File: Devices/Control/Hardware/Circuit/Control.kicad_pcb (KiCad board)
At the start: 2 copper layers, 53 parts, among them J1 Screw_Terminal_01x03, J2 Screw_Terminal_01x03, J3 Conn_01x04, J4 Conn_01x04, J5 Conn_01x04, J6 AVR-ISP-6, J7 TYPE-C-31-M-12, J8 TYPE-C-31-M-12, Q1 Q_NPN_BCE, SW1 SW_Push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

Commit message: First control PCB
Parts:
- removed the D2 at (31.2, 132.4)
- added C9: 100n, Capacitor_SMD:C_0805_2012Metric_Pad1.18x1.45mm_HandSolder, B.Cu at (176.0, 7.54)
- added R11: 10k, Resistor_SMD:R_0805_2012Metric_Pad1.20x1.40mm_HandSolder, B.Cu at (144.0, -5.66)
- added R12: 10k, Resistor_SMD:R_0805_2012Metric_Pad1.20x1.40mm_HandSolder, B.Cu at (176.0, -5.66)
- added R13: 10k, Resistor_SMD:R_0805_2012Metric_Pad1.20x1.40mm_HandSolder, B.Cu at (176.0, 0.94)
- C2, C4, JP1, JP10, JP11, JP12, JP13, JP14, JP15, JP16, JP2, JP3, JP4, JP5, JP6, JP7, JP8, JP9, R2, R7, U2, U3: moved to B.Cu
- moved R6 247.0 mm to (199.6, -25.8), turned to 270 degrees
- moved D2 245.8 mm to (194.5, -25.8), turned to 90 degrees
- moved JP15 224.2 mm to (177.3, -21.0)
- moved JP16 223.0 mm to (177.3, -15.8), turned to 180 degrees
- moved SW2 222.7 mm to (197.1, -30.4)
- moved JP13 221.9 mm to (169.7, -21.0)
- moved JP14 220.8 mm to (169.7, -15.8), turned to 180 degrees
- moved J7 213.5 mm to (160.3, -35.0), turned to 180 degrees
- moved JP11 212.2 mm to (150.6, -21.0), turned to 180 degrees
- moved JP12 211.0 mm to (150.6, -15.8)
- moved J6 208.6 mm to (182.2, 15.2)
- moved C3 206.2 mm to (144.0, -5.66)
- moved U4 202.7 mm to (160.3, -16.3)
- moved R2 200.3 mm to (144.0, 0.94), turned to 180 degrees
- moved C1 198.1 mm to (144.0, 10.1)
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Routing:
- net GND: track 0.00 -> 483.2 mm, vias 0 -> 14
- net VCC: track 0.00 -> 312.8 mm, vias 0 -> 7
- net RST: track 0.00 -> 163.7 mm, vias 0 -> 1
- net EXTRX: track 0.00 -> 147.7 mm, vias 0 -> 1
- net EXTTX: track 0.00 -> 120.5 mm, vias 0 -> 2
- net SCL: track 0.00 -> 100.3 mm, vias 0 -> 2
- net EXTRST: track 0.00 -> 97.9 mm
- net RX: track 0.00 -> 89.0 mm, vias 0 -> 1
- net SDA: track 0.00 -> 87.1 mm, vias 0 -> 1
- net XTAL1: track 0.00 -> 86.2 mm
- net TX: track 0.00 -> 65.6 mm, vias 0 -> 1
- net SIG1A: track 0.00 -> 48.9 mm
- net SIG1B: track 0.00 -> 48.4 mm
- net SIG2A: track 0.00 -> 43.9 mm, vias 0 -> 2
- net SIG2B: track 0.00 -> 43.5 mm, vias 0 -> 2
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- added copper zone on B.Cu, net GND
- added copper zone on F.Cu, net GND
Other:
- board outline added: 82.5 x 73 mm

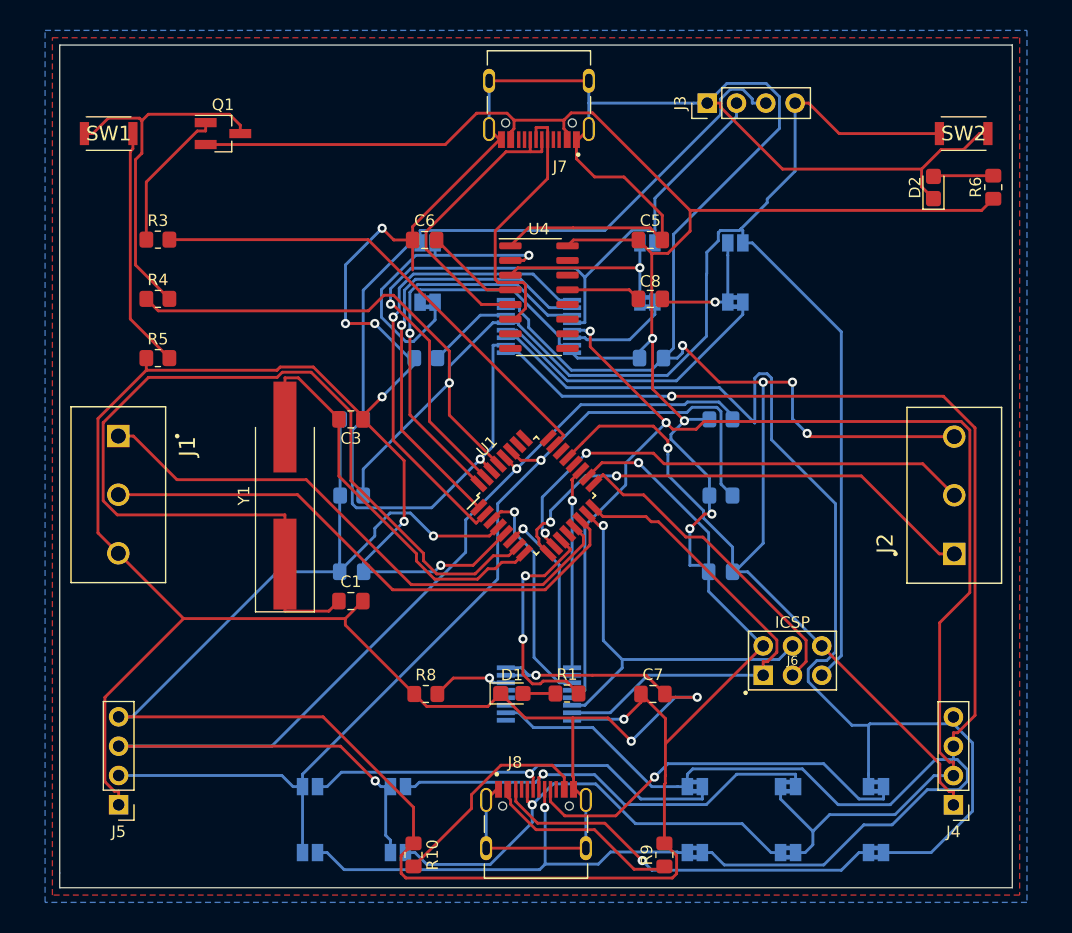
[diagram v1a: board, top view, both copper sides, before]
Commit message: Add mounting holes & component description
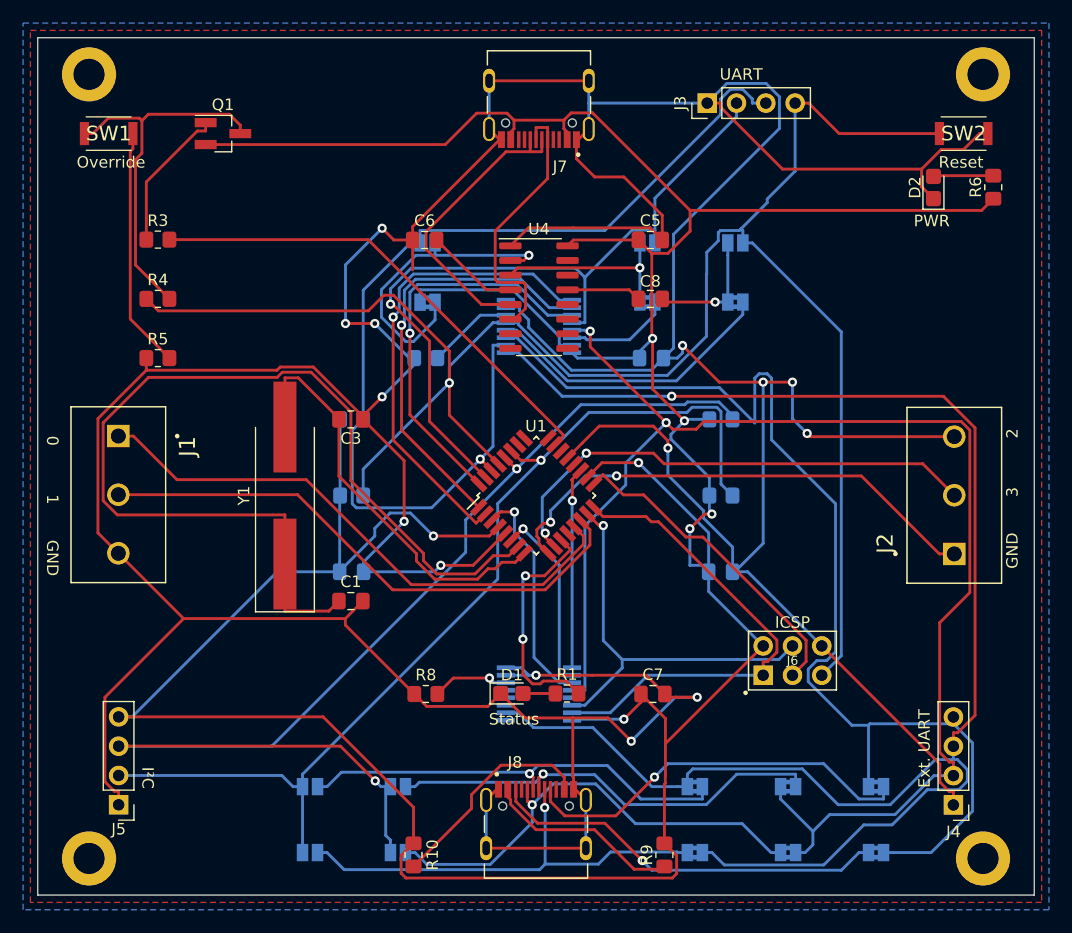
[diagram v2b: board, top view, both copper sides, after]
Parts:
- added MNT1: MountingHole_2.7mm_M2.5_DIN965_Pad, MountingHole:MountingHole_2.7mm_M2.5_DIN965_Pad, F.Cu at (198.8, 32.4)
- added MNT2: MountingHole_2.7mm_M2.5_DIN965_Pad, MountingHole:MountingHole_2.7mm_M2.5_DIN965_Pad, F.Cu at (121.3, 32.4)
- added MNT3: MountingHole_2.7mm_M2.5_DIN965_Pad, MountingHole:MountingHole_2.7mm_M2.5_DIN965_Pad, F.Cu at (121.3, -35.6)
- added MNT4: MountingHole_2.7mm_M2.5_DIN965_Pad, MountingHole:MountingHole_2.7mm_M2.5_DIN965_Pad, F.Cu at (198.8, -35.6)
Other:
- board size 82.5 x 73 mm -> 86.4 x 74.3 mm
- board text added: "0"
- board text added: "1"
- board text added: "2"
- board text added: "3"
- board text added: "Ext. UART"
- board text added: "GND"
- board text added: "I²C"
- board text added: "Override"
- board text added: "PWR"
- board text added: "Reset"
- board text added: "Status"
- board text added: "UART"
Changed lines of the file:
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@@
   (general
     (thickness 1.6)
-    (drawings 5)
+    (drawings 17)
     (tracks 858)
     (zones 0)
-    (modules 56)
+    (modules 60)
     (nets 78)
   )
@@
     (47 F.CrtYd user)
     (48 B.Fab user)
-    (49 F.Fab user)
+    (49 F.Fab user hide)
   )
   (setup
@@
     (add_net XTAL2)
   )
+  (module MountingHole:MountingHole_2.7mm_M2.5_DIN965_Pad (layer F.Cu)
+    (at 198.755 -35.56)
+    (descr "Mounting Hole 2.7mm, M2.5, DIN965")
+    (tags "mounting hole 2.7mm m2.5 din965")
+    (attr virtual)
+    (fp_text reference MNT4 (at 0 -3.35) (layer F.SilkS) hide
+      (effects (font (size 1 1) (thickness 0.15)))
+    )
+    (fp_text value MountingHole_2.7mm_M2.5_DIN965_Pad (at 0 3.35) (layer F.Fab)
+      (effects (font (size 1 1) (thickness 0.15)))
+    )
+    (fp_circle (center 0 0) (end 2.35 0) (layer Cmts.User) (width 0.15))
+    (fp_circle (center 0 0) (end 2.6 0) (layer F.CrtYd) (width 0.05))
+    (fp_text user %R (at 0.3 0) (layer F.Fab)
+      (effects (font (size 1 1) (thickness 0.15)))
+    )
+    (pad 1 thru_hole circle (at 0 0) (size 4.7 4.7) (drill 2.7) (layers *.Cu *.Mask))
+  )
+  (module MountingHole:MountingHole_2.7mm_M2.5_DIN965_Pad (layer F.Cu)
+    (at 121.285 -35.56)
+    (descr "Mounting Hole 2.7mm, M2.5, DIN965")
+    (tags "mounting hole 2.7mm m2.5 din965")
+    (attr virtual)
+    (fp_text reference MNT3 (at 0 -3.35) (layer F.SilkS) hide
+      (effects (font (size 1 1) (thickness 0.15)))
+    )
+    (fp_text value MountingHole_2.7mm_M2.5_DIN965_Pad (at 0 3.35) (layer F.Fab)
+      (effects (font (size 1 1) (thickness 0.15)))
+    )
+    (fp_circle (center 0 0) (end 2.35 0) (layer Cmts.User) (width 0.15))
+    (fp_circle (center 0 0) (end 2.6 0) (layer F.CrtYd) (width 0.05))
+    (fp_text user %R (at 0.3 0) (layer F.Fab)
+      (effects (font (size 1 1) (thickness 0.15)))
+    )
+    (pad 1 thru_hole circle (at 0 0) (size 4.7 4.7) (drill 2.7) (layers *.Cu *.Mask))
+  )
+  (module MountingHole:MountingHole_2.7mm_M2.5_DIN965_Pad (layer F.Cu)
+    (at 121.285 32.385)
+    (descr "Mounting Hole 2.7mm, M2.5, DIN965")
+    (tags "mounting hole 2.7mm m2.5 din965")
+    (attr virtual)
+    (fp_text reference MNT2 (at 0 -3.35) (layer F.SilkS) hide
+      (effects (font (size 1 1) (thickness 0.15)))
+    )
+    (fp_text value MountingHole_2.7mm_M2.5_DIN965_Pad (at 0 3.35) (layer F.Fab)
+      (effects (font (size 1 1) (thickness 0.15)))
+    )
+    (fp_circle (center 0 0) (end 2.35 0) (layer Cmts.User) (width 0.15))
+    (fp_circle (center 0 0) (end 2.6 0) (layer F.CrtYd) (width 0.05))
+    (fp_text user %R (at 0.3 0) (layer F.Fab)
+      (effects (font (size 1 1) (thickness 0.15)))
+    )
+    (pad 1 thru_hole circle (at 0 0) (size 4.7 4.7) (drill 2.7) (layers *.Cu *.Mask))
+  )
+  (module MountingHole:MountingHole_2.7mm_M2.5_DIN965_Pad (layer F.Cu)
+    (at 198.755 32.385)
+    (descr "Mounting Hole 2.7mm, M2.5, DIN965")
+    (tags "mounting hole 2.7mm m2.5 din965")
+    (attr virtual)
+    (fp_text reference MNT1 (at 0 -3.35) (layer F.SilkS) hide
+      (effects (font (size 1 1) (thickness 0.15)))
+    )
+    (fp_text value MountingHole_2.7mm_M2.5_DIN965_Pad (at 0 3.35) (layer F.Fab)
+      (effects (font (size 1 1) (thickness 0.15)))
+    )
+    (fp_text user %R (at 0.3 0) (layer F.Fab)
+      (effects (font (size 1 1) (thickness 0.15)))
+    )
+    (fp_circle (center 0 0) (end 2.35 0) (layer Cmts.User) (width 0.15))
+    (fp_circle (center 0 0) (end 2.6 0) (layer F.CrtYd) (width 0.05))
+    (pad 1 thru_hole circle (at 0 0) (size 4.7 4.7) (drill 2.7) (layers *.Cu *.Mask))
+  )
   (module Capacitor_SMD:C_0805_2012Metric_Pad1.18x1.45mm_HandSolder (layer B.Cu)
     (at 176.017 7.5438)
@@
       (effects (font (size 1 1) (thickness 0.15)) (justify mirror))
     )
-    (fp_text user %R (at 0 0) (layer B.Fab)
-      (effects (font (size 0.5 0.5) (thickness 0.08)) (justify mirror))
-    )
     (fp_line (start -1 -0.625) (end -1 0.625) (layer B.Fab) (width 0.1))
     (fp_line (start -1 0.625) (end 1 0.625) (layer B.Fab) (width 0.1))
@@
     (fp_line (start 1.88 0.98) (end 1.88 -0.98) (layer B.CrtYd) (width 0.05))
     (fp_line (start 1.88 -0.98) (end -1.88 -0.98) (layer B.CrtYd) (width 0.05))
+    (fp_text user %R (at 0 0) (layer B.Fab)
+      (effects (font (size 0.5 0.5) (thickness 0.08)) (justify mirror))
+    )
     (pad 2 smd roundrect (at 1.0375 0) (size 1.175 1.45) (layers B.Cu B.Paste B.Mask) (roundrect_rratio 0.212766)
       (net 2 GND))
@@
     (tags "QFP 0.8")
     (attr smd)
-    (fp_text reference U1 (at 0 -6.05 45) (layer F.SilkS)
+    (fp_text reference U1 (at 4.238964 -4.274319 180) (layer F.SilkS)
       (effects (font (size 1 1) (thickness 0.15)))
     )
@@
     (descr "Through hole straight pin header, 1x04, 2.54mm pitch, single row")
     (tags "Through hole pin header THT 1x04 2.54mm single row")
-    (fp_text reference J5 (at 0 -2.33) (layer F.SilkS)
+    (fp_text reference J5 (at 0 -2.1082) (layer F.SilkS)
       (effects (font (size 1 1) (thickness 0.15)))
     )
@@
     )
   )
-  (gr_line (start 201.295 -38.1) (end 201.295 34.925) (layer Edge.Cuts) (width 0.05))
-  (gr_line (start 118.745 34.925) (end 201.295 34.925) (layer Edge.Cuts) (width 0.05))
-  (gr_line (start 118.745 33.655) (end 118.745 34.925) (layer Edge.Cuts) (width 0.05))
-  (gr_line (start 118.745 -38.1) (end 118.745 33.655) (layer Edge.Cuts) (width 0.05))
-  (gr_line (start 201.295 -38.1) (end 118.745 -38.1) (layer Edge.Cuts) (width 0.05))
+  (gr_text PWR (at 194.31 -22.86) (layer F.SilkS)
+    (effects (font (size 1 1) (thickness 0.15)))
+  )
+  (gr_text Status (at 158.115 20.32) (layer F.SilkS)
+    (effects (font (size 1 1) (thickness 0.15)))
+  )
+  (gr_text Override (at 123.19 -27.94) (layer F.SilkS)
+    (effects (font (size 1 1) (thickness 0.15)))
+  )
+  (gr_text Reset (at 196.85 -27.94) (layer F.SilkS)
+    (effects (font (size 1 1) (thickness 0.15)))
+  )
+  (gr_text I²C (at 126.365 25.4 270) (layer F.SilkS)
+    (effects (font (size 1 1) (thickness 0.15)))
+  )
+  (gr_text "Ext. UART" (at 193.675 22.86 90) (layer F.SilkS)
+    (effects (font (size 1 1) (thickness 0.15)))
+  )
+  (gr_text UART (at 177.8 -35.56) (layer F.SilkS)
+    (effects (font (size 1 1) (thickness 0.15)))
+  )
+  (gr_text 2 (at 201.295 -4.445 90) (layer F.SilkS)
+    (effects (font (size 1 1) (thickness 0.15)))
+  )
+  (gr_text GND (at 201.295 5.715 90) (layer F.SilkS)
+    (effects (font (size 1 1) (thickness 0.15)))
+  )
+  (gr_text 3 (at 201.295 0.635 90) (layer F.SilkS)
+    (effects (font (size 1 1) (thickness 0.15)))
+  )
+  (gr_text 0 (at 118.11 -3.81 -90) (layer F.SilkS)
+    (effects (font (size 1 1) (thickness 0.15)))
+  )
+  (gr_text 1 (at 118.11 1.27 -90) (layer F.SilkS)
+    (effects (font (size 1 1) (thickness 0.15)))
+  )
+  (gr_text GND (at 118.11 6.35 270) (layer F.SilkS)
+    (effects (font (size 1 1) (thickness 0.15)))
+  )
+  (gr_line (start 203.2 -38.735) (end 203.2 35.56) (layer Edge.Cuts) (width 0.05))
+  (gr_line (start 116.84 35.56) (end 203.2 35.56) (layer Edge.Cuts) (width 0.05))
+  (gr_line (start 116.84 -38.735) (end 116.84 35.56) (layer Edge.Cuts) (width 0.05))
+  (gr_line (start 203.2 -38.735) (end 116.84 -38.735) (layer Edge.Cuts) (width 0.05))
   (segment (start 138.262 2.6145) (end 123.733 2.6145) (width 0.25) (layer F.Cu) (net 1))
   (segment (start 123.733 2.6145) (end 122.5096 1.3911) (width 0.25) (layer F.Cu) (net 1))
@@
   (segment (start 156.2937 17.0561) (end 155.9897 16.7521) (width 0.25) (layer B.Cu) (net 63))
   (via (at 155.9897 16.7521) (size 0.8) (layers F.Cu B.Cu) (net 63))
-  (zone (net 2) (net_name GND) (layer F.Cu) (hatch edge 0.508)
+  (zone (net 2) (net_name GND) (layer B.Cu) (hatch edge 0.508)
     (connect_pads (clearance 0.508))
     (min_thickness 0.254)
@@
     (polygon
       (pts
-        (xy 201.93 35.56) (xy 118.11 35.56) (xy 118.11 -38.735) (xy 201.93 -38.735)
+        (xy 204.47 36.83) (xy 115.57 36.83) (xy 115.57 -40.005) (xy 204.47 -40.005)
       )
     )
   )
-  (zone (net 2) (net_name GND) (layer B.Cu) (hatch edge 0.508)
+  (zone (net 2) (net_name GND) (layer F.Cu) (hatch edge 0.508)
     (connect_pads (clearance 0.508))
     (min_thickness 0.254)
@@
     (polygon
       (pts
-        (xy 202.565 36.195) (xy 117.475 36.195) (xy 117.475 -39.37) (xy 202.565 -39.37)
+        (xy 203.835 36.195) (xy 116.205 36.195) (xy 116.205 -39.37) (xy 203.835 -39.37)
       )
     )

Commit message: Add version number & author information
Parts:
- moved C1 95.6 mm to (131.8, 105.0)
- moved C2 95.6 mm to (131.9, 102.4)
- moved C3 95.6 mm to (131.8, 89.2)
- moved C4 95.6 mm to (157.8, 83.9)
- moved C5 95.6 mm to (157.7, 73.7)
- moved C6 95.6 mm to (138.2, 73.7)
- moved C7 95.6 mm to (158.0, 113.0)
- moved C8 95.6 mm to (157.7, 78.8)
- moved C9 95.6 mm to (163.8, 102.4)
- moved D1 95.6 mm to (145.7, 113.0)
- moved D2 95.6 mm to (182.3, 69.1)
- moved J1 95.6 mm to (111.6, 90.7)
- moved J2 95.6 mm to (184.1, 100.9)
- moved J3 95.6 mm to (162.7, 61.8)
- moved J4 95.6 mm to (184.0, 122.6)
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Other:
- board text added: "29.08.2021"
- board text added: "Designed by: GHOSCHT"
- board text added: "V01"

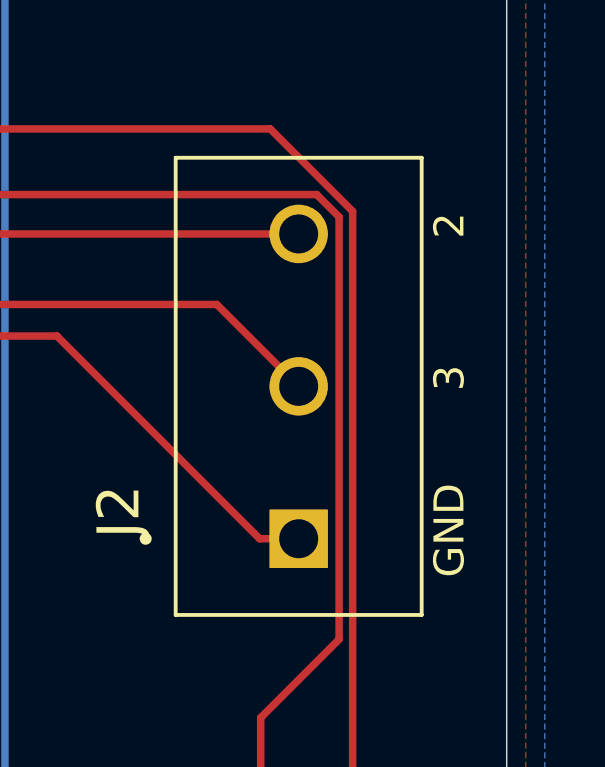
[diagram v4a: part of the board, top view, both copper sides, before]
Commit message: Fix output port numbering
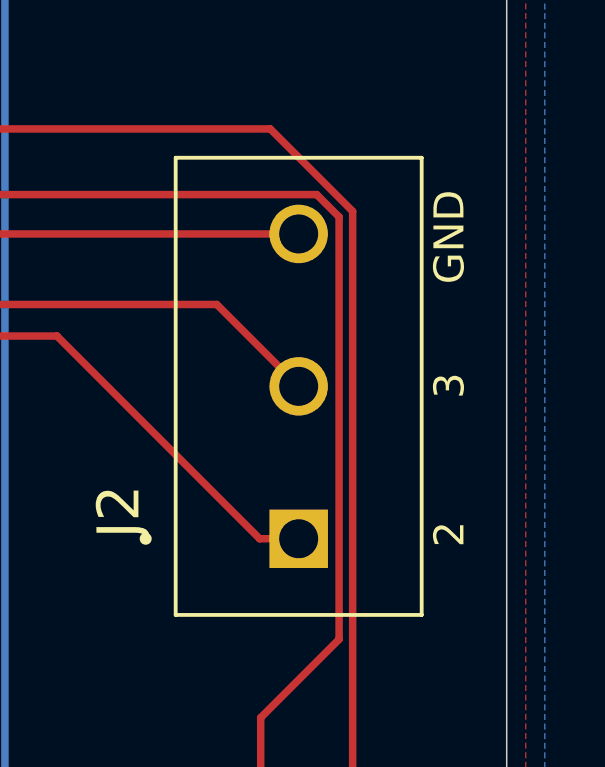
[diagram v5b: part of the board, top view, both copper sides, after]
